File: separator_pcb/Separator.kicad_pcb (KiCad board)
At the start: 2 copper layers, 32 x 8 mm, 10 parts, among them J1 L_COL_CONN, Q1 BSS138

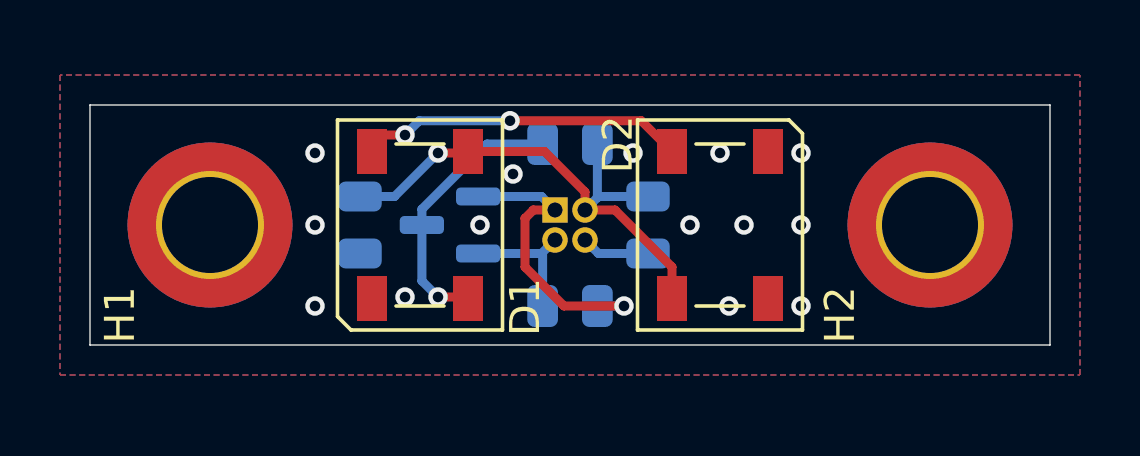
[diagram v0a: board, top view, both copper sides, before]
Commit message: Footprint placement done, PWR needs connecting
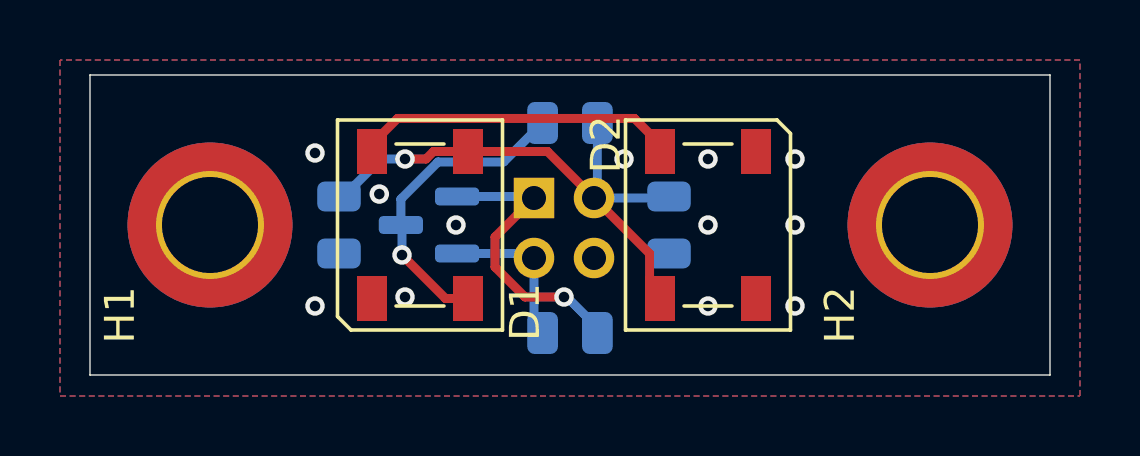
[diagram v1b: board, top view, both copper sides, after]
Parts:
- J1: value L_COL_CONN -> COL_CONN; footprint Connector_PinHeader_1.00mm:PinHeader_2x02_P1.00mm_Vertical -> Connector_PinHeader_2.00mm:PinHeader_2x02_P2.00mm_Vertical
- moved R1 0.90 mm to (140.0, 115.6)
- moved J1 0.81 mm to (138.8, 111.1)
- moved C1 0.70 mm to (143.3, 112.0)
- moved R2 0.70 mm to (140.0, 108.6)
- moved C2 0.70 mm to (132.3, 112.0)
- moved Q1 0.70 mm to (135.3, 112.0)
- moved D2 0.40 mm to (144.6, 112.0)
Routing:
- net GND: track 2.29 -> 0.00 mm, vias 14 -> 12
- net Net-(D1-DIN): track 9.09 -> 10.5 mm
- net +5V: track 18.1 -> 19.1 mm
- net /COLON_LED: track 4.51 -> 5.24 mm
- net Net-(D1-DO): track 10.5 -> 10.3 mm, vias 2 -> 0
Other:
- board size 32 x 8 mm -> 32 x 10 mm

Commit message: Layout done, generated fabrication files
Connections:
- H1 pad 1: unconnected-(H1-Pad1)_2 -> GND
- H2 pad 1: unconnected-(H2-Pad1) -> GND
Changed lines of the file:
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@@
 	(net 5 "Net-(D1-DO)")
 	(net 6 "unconnected-(D2-DO-Pad4)")
-	(net 7 "unconnected-(H1-Pad1)")
-	(net 8 "unconnected-(H1-Pad1)_1")
-	(net 9 "unconnected-(H1-Pad1)_2")
-	(net 10 "unconnected-(H2-Pad1)")
-	(net 11 "unconnected-(H2-Pad1)_1")
-	(net 12 "unconnected-(H2-Pad1)_2")
-	(net 13 "/COLON_LED")
+	(net 7 "/COLON_LED")
 	(footprint "LED_SMD:LED_Inolux_IN-PI554FCH_PLCC4_5.0x5.0mm_P3.2mm"
 		(layer "F.Cu")
@@
 			(layers "*.Cu" "*.Mask")
 			(remove_unused_layers no)
-			(net 8 "unconnected-(H1-Pad1)_1")
+			(net 1 "GND")
 			(pinfunction "1")
-			(pintype "input+no_connect")
+			(pintype "input")
 		)
 		(pad "1" connect circle
@@
 			(size 5.5 5.5)
 			(layers "F.Cu" "F.Mask")
-			(net 7 "unconnected-(H1-Pad1)")
+			(net 1 "GND")
 			(pinfunction "1")
-			(pintype "input+no_connect")
+			(pintype "input")
 		)
 		(pad "1" connect circle
@@
 			(size 5.5 5.5)
 			(layers "B.Cu" "B.Mask")
-			(net 9 "unconnected-(H1-Pad1)_2")
+			(net 1 "GND")
 			(pinfunction "1")
-			(pintype "input+no_connect")
+			(pintype "input")
 		)
 		(embedded_fonts no)
@@
 			(layers "*.Cu" "*.Mask")
 			(remove_unused_layers no)
-			(net 11 "unconnected-(H2-Pad1)_1")
+			(net 1 "GND")
 			(pinfunction "1")
-			(pintype "input+no_connect")
+			(pintype "input")
 		)
 		(pad "1" connect circle
@@
 			(size 5.5 5.5)
 			(layers "F.Cu" "F.Mask")
-			(net 12 "unconnected-(H2-Pad1)_2")
+			(net 1 "GND")
 			(pinfunction "1")
-			(pintype "input+no_connect")
+			(pintype "input")
 		)
 		(pad "1" connect circle
@@
 			(size 5.5 5.5)
 			(layers "B.Cu" "B.Mask")
-			(net 10 "unconnected-(H2-Pad1)")
+			(net 1 "GND")
 			(pinfunction "1")
-			(pintype "input+no_connect")
+			(pintype "input")
 		)
 		(embedded_fonts no)
@@
 			(layers "*.Cu" "*.Mask")
 			(remove_unused_layers no)
-			(net 13 "/COLON_LED")
+			(net 7 "/COLON_LED")
 			(pinfunction "Pin_2")
 			(pintype "passive")
@@
 			(layers "B.Cu" "B.Mask" "B.Paste")
 			(roundrect_rratio 0.25)
-			(net 13 "/COLON_LED")
+			(net 7 "/COLON_LED")
 			(pinfunction "S")
 			(pintype "passive")
@@
 			(layers "B.Cu" "B.Mask" "B.Paste")
 			(roundrect_rratio 0.243902)
-			(net 13 "/COLON_LED")
+			(net 7 "/COLON_LED")
 			(pintype "passive")
 		)
@@
 		(width 0.3)
 		(layer "B.Cu")
-		(net 13)
+		(net 7)
 	)
 	(segment
@@
 		(width 0.3)
 		(layer "B.Cu")
-		(net 13)
+		(net 7)
 	)
 	(segment
@@
 		(width 0.3)
 		(layer "B.Cu")
-		(net 13)
+		(net 7)
 	)
 	(segment
@@
 		(width 0.3)
 		(layer "B.Cu")
-		(net 13)
+		(net 7)
 	)
 	(zone
